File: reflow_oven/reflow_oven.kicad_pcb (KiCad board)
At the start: 2 copper layers, 49 x 58.2 mm, 30 parts, among them J1 UART, J2 POWER, J3 LED, J4 K-TYPE, J5 BUTTON1, J6 BUTTON2, J7 RELAY, J8 I2C, Q1 2n2222, U1 ATmega328-PU, U2 MAX6675, Y1 16MHz

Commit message: Updated Design
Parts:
- added C10: 100n, Capacitor_SMD:C_0805_2012Metric, F.Cu at (60.7, 62.2)
- added D1: MBR0540T1G, Diode_SMD:D_SOD-123, F.Cu at (63.0, 80.8)
- added J10: FAN, Connector_Molex:Molex_KK-254_AE-6410-02A_1x02_P2.54mm_Vertical, F.Cu at (68.1, 75.9)
- added J9: BUTTON3, Connector_Molex:Molex_KK-254_AE-6410-02A_1x02_P2.54mm_Vertical, F.Cu at (56.6, 56.9)
- added Q2: 2n2222, Package_TO_SOT_THT:TO-92_Inline, F.Cu at (62.0, 75.9)
- added R6: 1k, Resistor_SMD:R_0805_2012Metric, F.Cu at (56.6, 62.2)
- added R7: 1k, Resistor_SMD:R_0805_2012Metric, F.Cu at (60.2, 79.8)
- J1, J8: footprint Connector_Molex:Molex_KK-396_A-41791-0004_1x04_P3.96mm_Vertical -> Connector_Molex:Molex_KK-254_AE-6410-04A_1x04_P2.54mm_Vertical
- J2, J3, J4, J5, J6, J7: footprint Connector_Molex:Molex_KK-396_A-41791-0002_1x02_P3.96mm_Vertical -> Connector_Molex:Molex_KK-254_AE-6410-02A_1x02_P2.54mm_Vertical
- moved J1 15.7 mm to (33.8, 74.2), turned to 90 degrees
- moved J4 7.84 mm to (68.1, 83.1)
- moved H1 6.86 mm to (32.8, 101.9)
- moved H4 6.84 mm to (32.8, 54.9)
- moved J7 6.84 mm to (33.8, 95.5)
- moved J8 6.59 mm to (68.1, 63.8), turned to 270 degrees
- moved J3 4.52 mm to (33.8, 88.4)
- moved H2 3.71 mm to (68.9, 54.9)
- moved J2 3.57 mm to (33.8, 81.3)
- moved J6 2.79 mm to (47.6, 56.9)
- moved R2 2.70 mm to (40.1, 96.3), turned to 90 degrees
- moved C9 2.41 mm to (51.7, 62.2)
- moved R5 2.41 mm to (47.6, 62.2)
- moved C7 2.41 mm to (63.8, 92.7)
- moved J5 2.27 mm to (38.6, 56.9)
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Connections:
- C1 pad 1: +5V -> FAN_CONN+
- C2 pad 1: +5V -> FAN_CONN+
- C3 pad 1: +5V -> FAN_CONN+
- C7 pad 1: +5V -> FAN_CONN+
- J1 pad 1: RST -> UART_TX
- J1 pad 3: UART_TX -> RST
- J2 pad 1: +5V -> FAN_CONN+
- J7 pad 1: RELAY_CONN -> FAN_CONN+
- J7 pad 2: GND -> RELAY_CONN
- J8 pad 1: SDA -> FAN_CONN+
- J8 pad 2: SCL -> SDA
- J8 pad 3: +5V -> SCL
- R1 pad 1: +5V -> FAN_CONN+
- U1 pad 20: +5V -> FAN_CONN+
- U1 pad 23: Net-(U1-Pad23) -> FAN
- U1 pad 6: Net-(U1-Pad6) -> BUTTON3
- U1 pad 7: +5V -> FAN_CONN+
- U2 pad 4: +5V -> FAN_CONN+
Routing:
- net FAN_CONN+: track 0.00 -> 107.7 mm, vias 0 -> 2
- net +5V: track 94.7 -> 0.00 mm, vias 2 -> 0
- net BUTTON3: track 0.00 -> 25.1 mm
- net FAN_CONN-: track 0.00 -> 9.20 mm
- net GND: track 28.3 -> 37.5 mm, vias 9 -> 8
- net K-: track 16.7 -> 9.34 mm
- net K+: track 11.3 -> 4.98 mm
- net UART_RX: track 23.1 -> 16.9 mm
- net RST: track 23.6 -> 17.5 mm
- net Net-(Q2-Pad2): track 0.00 -> 5.77 mm
- net BUTTON3_CONN: track 0.00 -> 5.72 mm
- net UART_TX: track 22.5 -> 16.9 mm
- net RELAY: track 17.3 -> 12.8 mm
- net FAN: track 0.00 -> 2.72 mm
- net BUTTON2_CONN: track 7.80 -> 5.72 mm
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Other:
- board size 49 x 58.2 mm -> 44.2 x 54.6 mm
- board text added: "BUTTON3"
- board text added: "FAN"

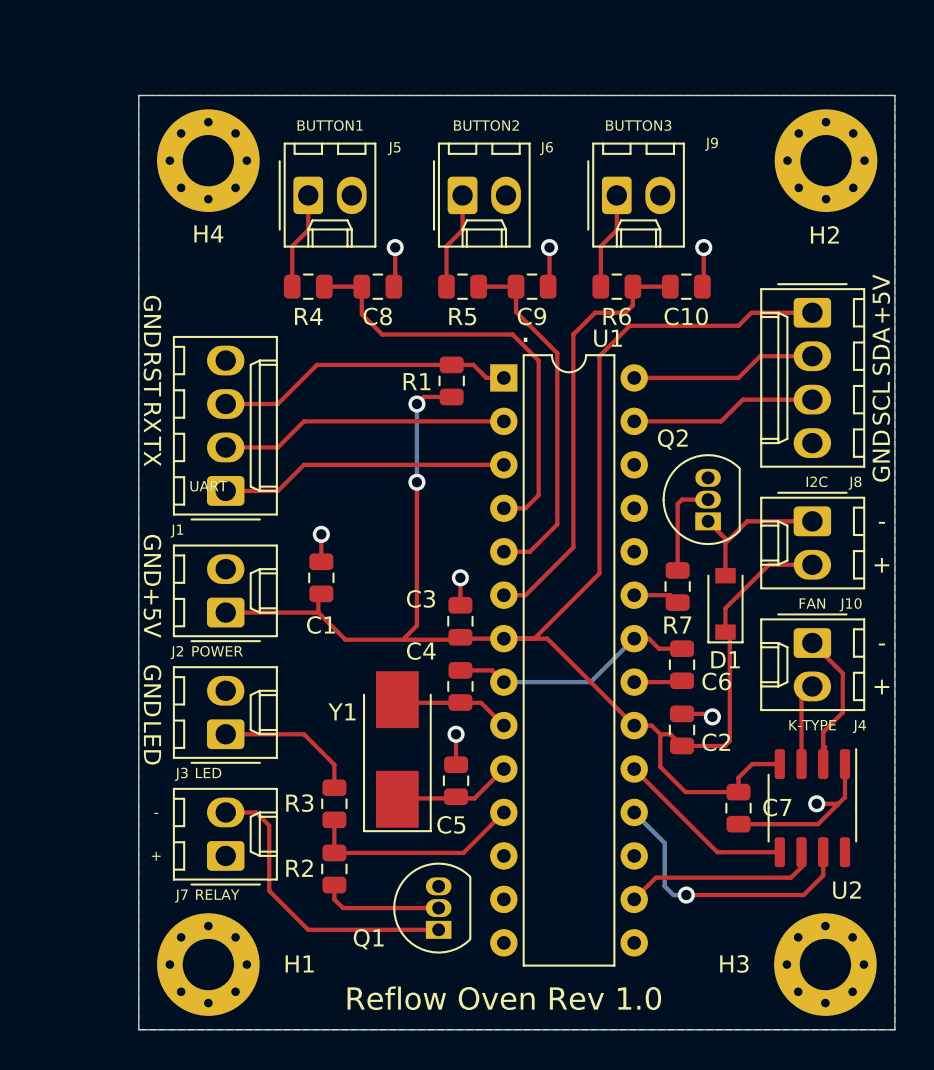
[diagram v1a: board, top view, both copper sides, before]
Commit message: Added SMD Crystal
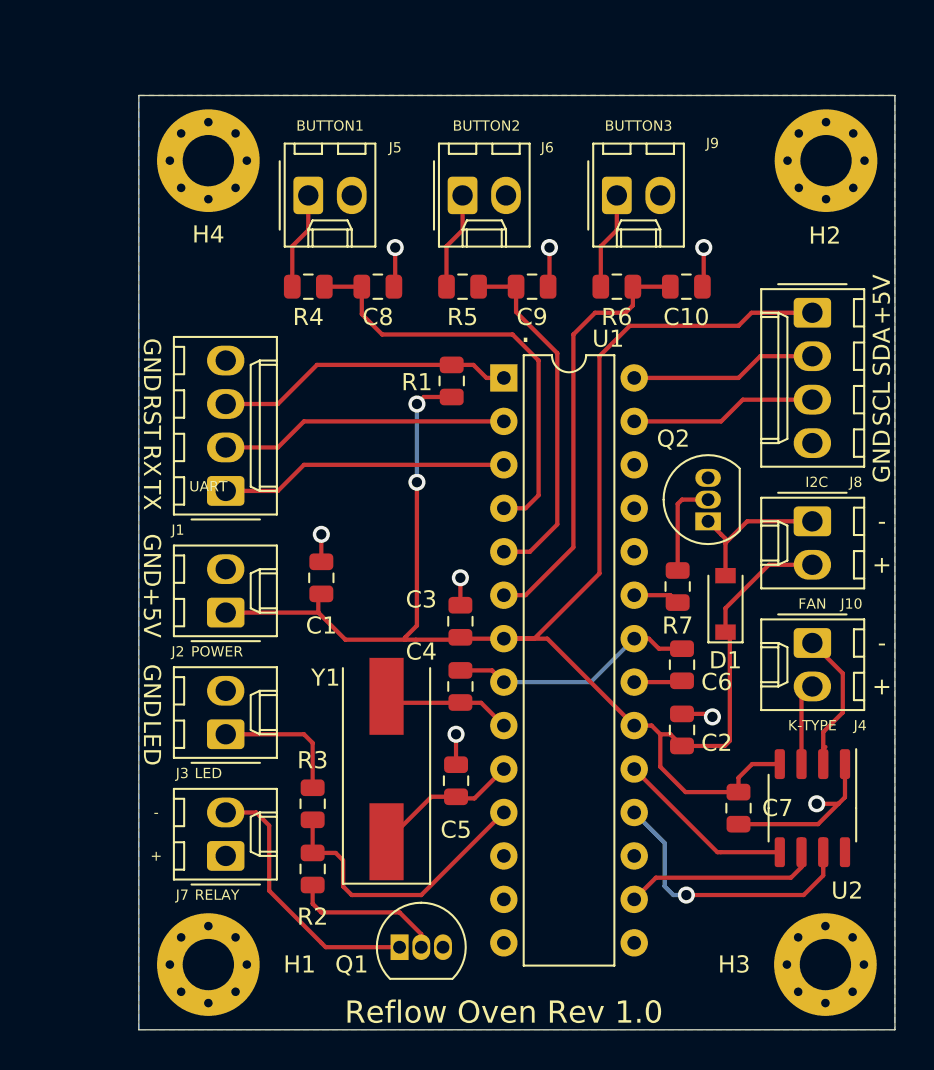
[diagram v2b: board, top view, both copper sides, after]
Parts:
- Y1: footprint Crystal:Crystal_SMD_0603-2Pin_6.0x3.5mm_HandSoldering -> Crystal:Crystal_SMD_HC49-SD
- moved Q1 2.50 mm to (43.9, 100.8), turned to 0 degrees
- moved Y1 1.31 mm to (43.2, 90.4)
- moved R2 1.27 mm to (38.9, 96.3)
- moved R3 1.27 mm to (38.9, 92.5)
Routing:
- net RELAY: track 12.8 -> 17.0 mm
- net RELAY_CONN: track 17.5 -> 15.7 mm
- net Net-(Q1-Pad2): track 7.15 -> 8.94 mm
- net XTAL2: track 6.96 -> 8.28 mm
- net LED_CONN: track 8.43 -> 7.91 mm

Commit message: Fina ldesign
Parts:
- added D2: ONLED, LED_SMD:LED_1206_3216Metric, F.Cu at (41.7, 74.7)
- added R8: 330, Resistor_SMD:R_0805_2012Metric, F.Cu at (42.7, 80.3)
- moved Q1 2.03 mm to (41.9, 100.8)
- moved C1 0.51 mm to (38.9, 79.2)
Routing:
- net FAN_CONN+: track 107.7 -> 127.1 mm
- net Net-(D2-Pad2): track 0.00 -> 4.81 mm
- net GND: track 37.5 -> 39.6 mm, vias 8 -> 9
- net RELAY_CONN: track 15.7 -> 13.6 mm
- net Net-(Q1-Pad2): track 8.94 -> 7.06 mm
- net LED_CONN: track 7.91 -> 7.31 mm
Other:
- rule trace_min: 0.2 -> 0.25
- rule via_min_size: 0.4 -> 0.6
